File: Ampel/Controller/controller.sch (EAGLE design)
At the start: 8 parts, among them IC1 ATtiny25

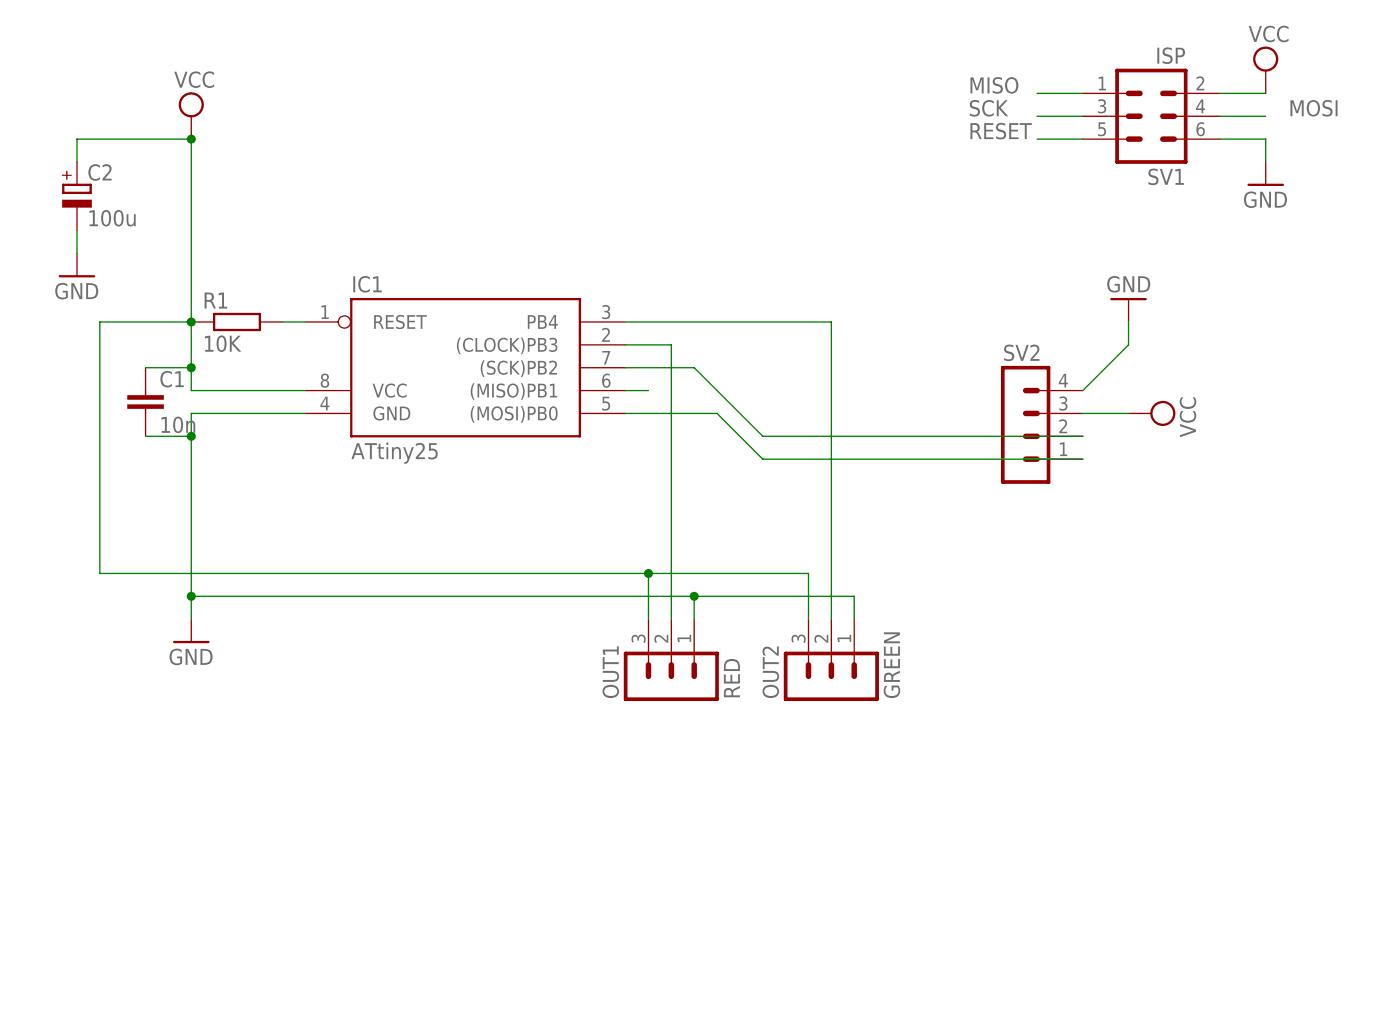
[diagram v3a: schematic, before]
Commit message: Adapter: stecker angepasst Controller: board redesign
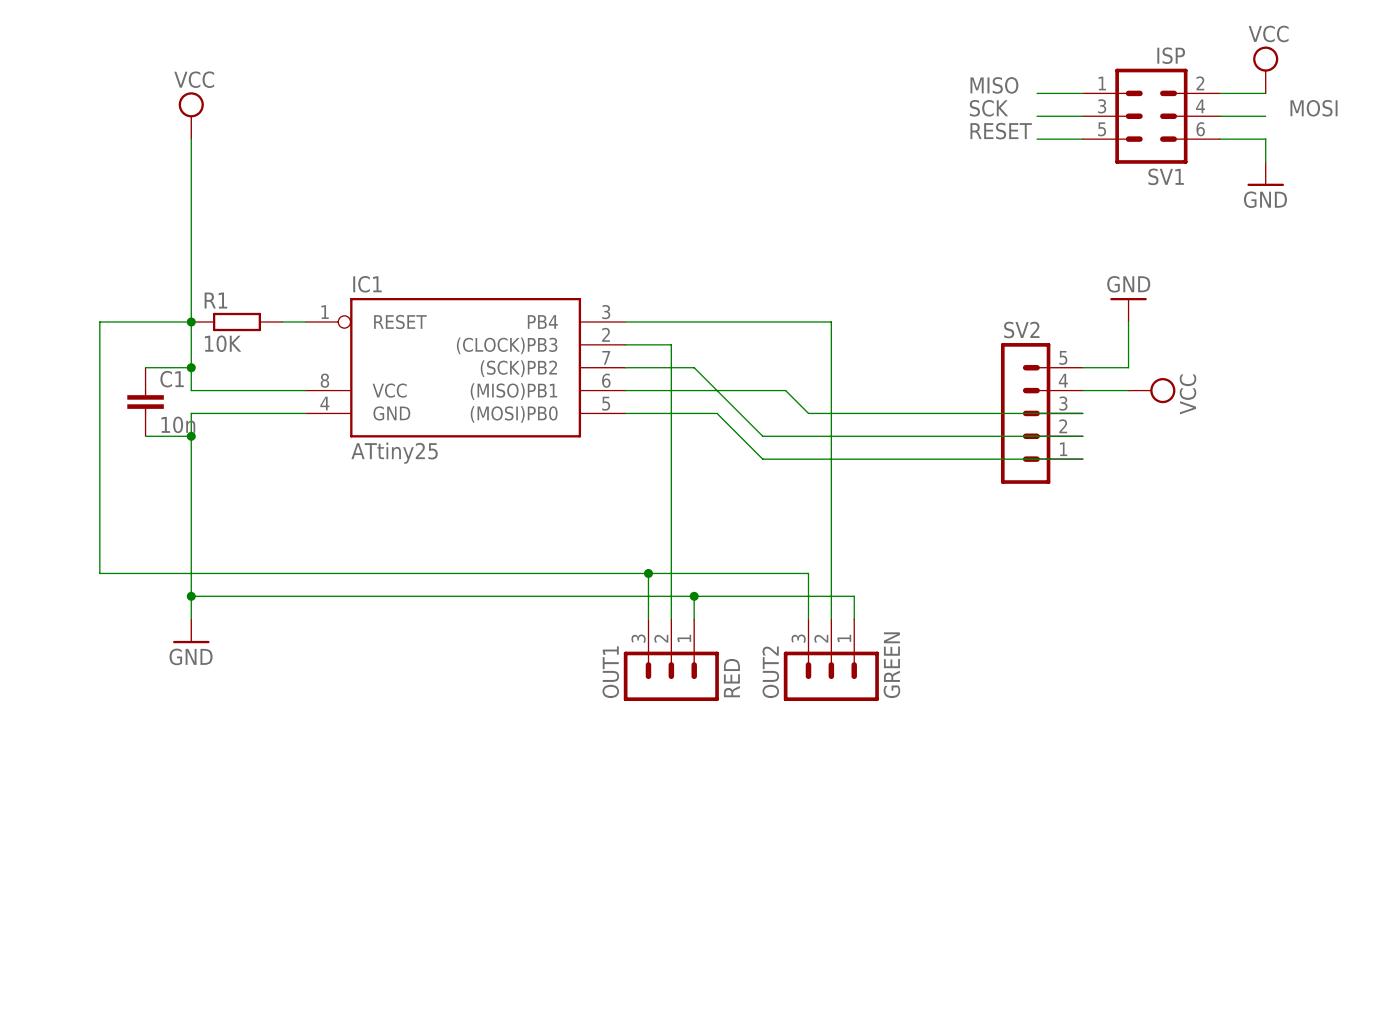
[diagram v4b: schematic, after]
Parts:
- removed C2: 100u, resistor:CPOL-EUE2.5-7
- R1: device resistor:R-EU_0207/10 -> resistor:R-EU_0207/7
- SV2: device con-lstb:MA04-1 -> con-lstb:MA05-1
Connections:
- net GND: now also SV2.5; no longer C2.-, SV2.4
- net MISO: now also SV2.3
- net VCC: now also SV2.4; no longer C2.+, SV2.3
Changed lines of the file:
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@@
 <part name="GND2" library="supply1" deviceset="GND" device=""/>
 <part name="IC1" library="atmel" deviceset="AT90*2343" device="P" technology="S" value="ATtiny25"/>
-<part name="R1" library="resistor" deviceset="R-EU_" device="0207/10" value="10K"/>
+<part name="R1" library="resistor" deviceset="R-EU_" device="0207/7" value="10K"/>
 <part name="C1" library="resistor" deviceset="C-EU" device="025-024X044" value="10n"/>
 <part name="SV1" library="con-lstb" deviceset="MA03-2" device="" value="ISP"/>
@@
 <part name="OUT1" library="con-lstb" deviceset="MA03-1" device="" value="RED"/>
 <part name="OUT2" library="con-lstb" deviceset="MA03-1" device="" value="GREEN"/>
-<part name="C2" library="resistor" deviceset="CPOL-EU" device="E2.5-7" value="100u"/>
-<part name="GND3" library="supply1" deviceset="GND" device=""/>
-<part name="SV2" library="con-lstb" deviceset="MA04-1" device=""/>
+<part name="SV2" library="con-lstb" deviceset="MA05-1" device=""/>
 <part name="GND4" library="supply1" deviceset="GND" device=""/>
 <part name="SUPPLY3" library="supply2" deviceset="VCC" device=""/>
@@
 <instance part="OUT1" gate="G$1" x="33.02" y="-5.08" rot="R90"/>
 <instance part="OUT2" gate="G$1" x="50.8" y="-5.08" rot="R90"/>
-<instance part="C2" gate="G$1" x="-33.02" y="50.8"/>
-<instance part="GND3" gate="1" x="-33.02" y="40.64"/>
-<instance part="SV2" gate="1" x="71.12" y="25.4"/>
+<instance part="SV2" gate="G$1" x="71.12" y="25.4"/>
 <instance part="GND4" gate="1" x="83.82" y="38.1" rot="R180"/>
-<instance part="SUPPLY3" gate="G$1" x="86.36" y="25.4" rot="R270"/>
+<instance part="SUPPLY3" gate="G$1" x="86.36" y="27.94" rot="R270"/>
 </instances>
 <busses>
@@
 <wire x1="-30.48" y1="7.62" x2="-30.48" y2="35.56" width="0.1524" layer="91"/>
 <wire x1="-30.48" y1="35.56" x2="-20.32" y2="35.56" width="0.1524" layer="91"/>
-<pinref part="C2" gate="G$1" pin="+"/>
-<wire x1="-33.02" y1="53.34" x2="-33.02" y2="55.88" width="0.1524" layer="91"/>
-<wire x1="-33.02" y1="55.88" x2="-20.32" y2="55.88" width="0.1524" layer="91"/>
-<junction x="-20.32" y="55.88"/>
 </segment>
 <segment>
@@
 <segment>
 <pinref part="SUPPLY3" gate="G$1" pin="VCC"/>
-<pinref part="SV2" gate="1" pin="3"/>
-<wire x1="83.82" y1="25.4" x2="78.74" y2="25.4" width="0.1524" layer="91"/>
+<pinref part="SV2" gate="G$1" pin="4"/>
+<wire x1="83.82" y1="27.94" x2="78.74" y2="27.94" width="0.1524" layer="91"/>
 </segment>
 </net>
@@
 </segment>
 <segment>
-<pinref part="GND3" gate="1" pin="GND"/>
-<pinref part="C2" gate="G$1" pin="-"/>
-<wire x1="-33.02" y1="43.18" x2="-33.02" y2="45.72" width="0.1524" layer="91"/>
-</segment>
-<segment>
-<pinref part="SV2" gate="1" pin="4"/>
 <pinref part="GND4" gate="1" pin="GND"/>
-<wire x1="78.74" y1="27.94" x2="83.82" y2="33.02" width="0.1524" layer="91"/>
-<wire x1="83.82" y1="33.02" x2="83.82" y2="35.56" width="0.1524" layer="91"/>
+<wire x1="83.82" y1="35.56" x2="83.82" y2="30.48" width="0.1524" layer="91"/>
+<pinref part="SV2" gate="G$1" pin="5"/>
+<wire x1="83.82" y1="30.48" x2="78.74" y2="30.48" width="0.1524" layer="91"/>
 </segment>
 </net>
@@
 <segment>
 <pinref part="IC1" gate="G$1" pin="(MISO)PB1"/>
-<wire x1="27.94" y1="27.94" x2="30.48" y2="27.94" width="0.1524" layer="91"/>
+<wire x1="27.94" y1="27.94" x2="45.72" y2="27.94" width="0.1524" layer="91"/>
+<wire x1="45.72" y1="27.94" x2="48.26" y2="25.4" width="0.1524" layer="91"/>
+<pinref part="SV2" gate="G$1" pin="3"/>
+<wire x1="48.26" y1="25.4" x2="78.74" y2="25.4" width="0.1524" layer="91"/>
 </segment>
 </net>
@@
 <wire x1="27.94" y1="30.48" x2="35.56" y2="30.48" width="0.1524" layer="91"/>
 <wire x1="35.56" y1="30.48" x2="43.18" y2="22.86" width="0.1524" layer="91"/>
-<pinref part="SV2" gate="1" pin="2"/>
+<pinref part="SV2" gate="G$1" pin="2"/>
 <wire x1="43.18" y1="22.86" x2="78.74" y2="22.86" width="0.1524" layer="91"/>
 </segment>
@@
 <wire x1="27.94" y1="25.4" x2="38.1" y2="25.4" width="0.1524" layer="91"/>
 <wire x1="38.1" y1="25.4" x2="43.18" y2="20.32" width="0.1524" layer="91"/>
-<pinref part="SV2" gate="1" pin="1"/>
+<pinref part="SV2" gate="G$1" pin="1"/>
 <wire x1="43.18" y1="20.32" x2="78.74" y2="20.32" width="0.1524" layer="91"/>
 </segment>
